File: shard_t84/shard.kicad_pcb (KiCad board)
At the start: 2 copper layers, 35 x 25 mm, 8 parts, among them J0 Shard, J1 ISP, U1 ATtiny84-20PU

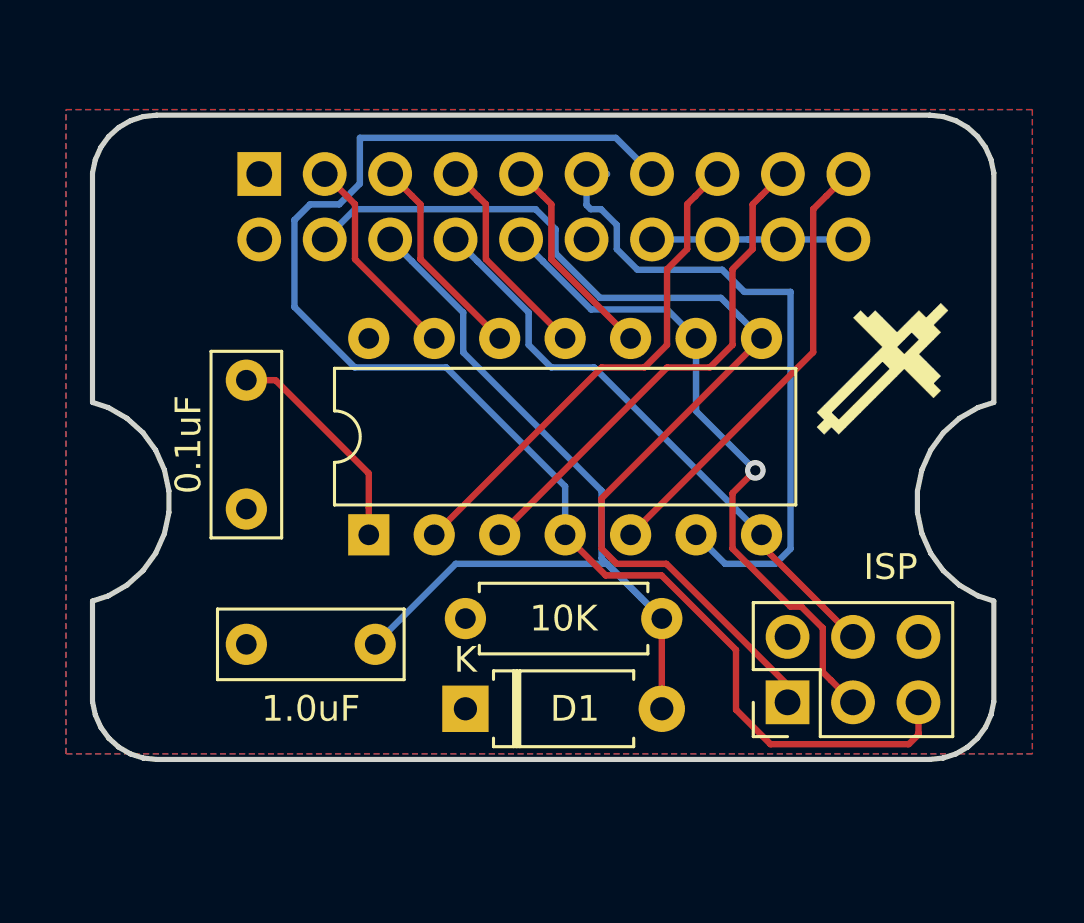
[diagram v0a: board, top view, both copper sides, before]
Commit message: reworked board for correct connector orientation
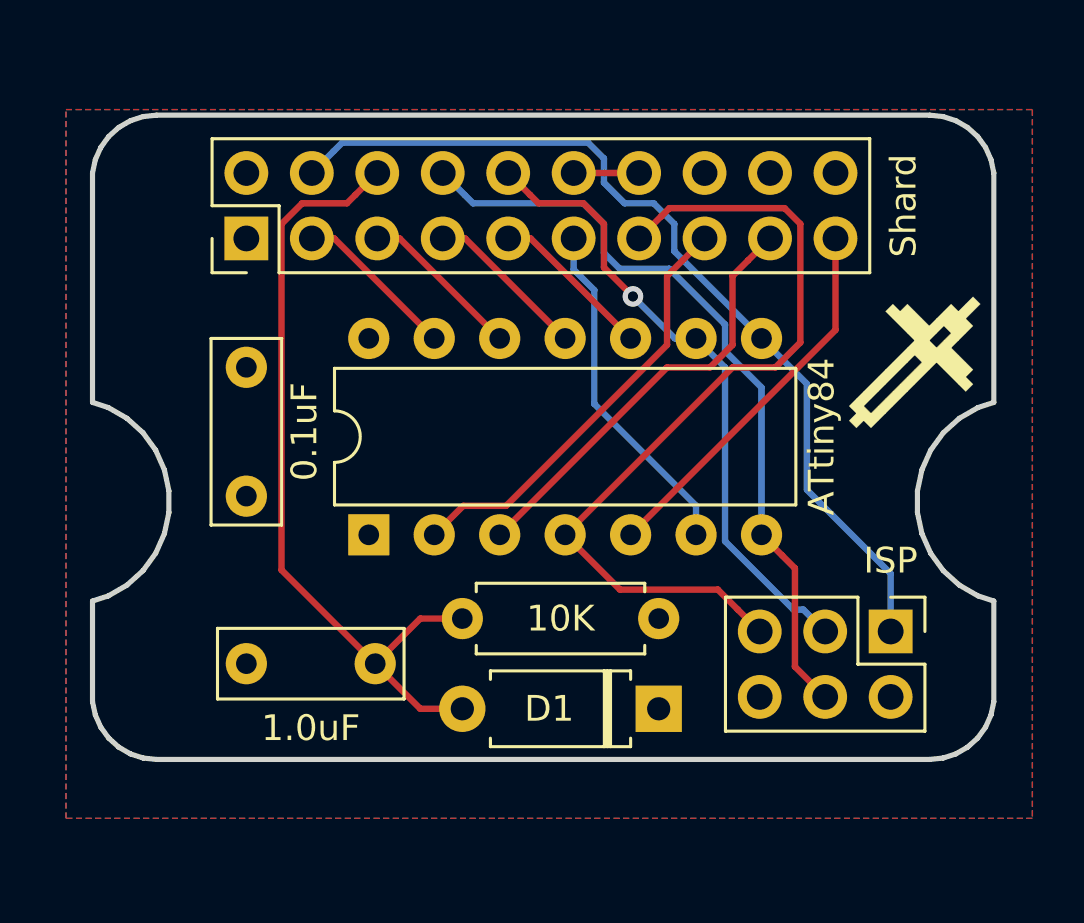
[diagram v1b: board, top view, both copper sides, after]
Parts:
- J0: moved to F.Cu
- U1: value ATtiny84-20PU -> ATtiny84
- moved D1 7.50 mm to (140.5, 75.8), turned to 180 degrees
- moved R1 7.50 mm to (140.5, 72.2), turned to 180 degrees
- moved J1 4.85 mm to (149.5, 72.8), turned to 270 degrees
- moved C0 4.50 mm to (124.5, 67.5), turned to 90 degrees
- moved J0 2.55 mm to (124.5, 57.5), turned to 90 degrees
- moved SPIKE 1.27 mm to (151.0, 57.5)
- moved C1 0.75 mm to (124.5, 74.0)
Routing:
- net RESET: track 55.3 -> 32.9 mm
- net SND: track 26.2 -> 13.5 mm
- net +3V3: track 8.63 -> 0.00 mm
- net D_MOSI: track 22.8 -> 30.1 mm
- net D_DC: track 40.9 -> 35.7 mm
- net GND: track 7.62 -> 2.54 mm
- net D_RST: track 35.9 -> 31.3 mm
- net BTN_A: track 17.5 -> 14.8 mm
- net BTN_B: track 19.5 -> 16.8 mm
- net BTN_C: track 19.5 -> 16.8 mm
- net DOWN: track 8.14 -> 6.36 mm
- net UP: track 8.14 -> 6.36 mm
- net RIGHT: track 8.14 -> 6.36 mm
- net LEFT: track 8.14 -> 6.36 mm
- net D_SCK: track 26.0 -> 24.6 mm
- added copper zone on F.Cu, net +3V3
- added copper zone on B.Cu, net GND
- removed copper zone on B.Cu, net +3V3
- removed copper zone on F.Cu, net GND

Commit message: t84 shard updated for new layout
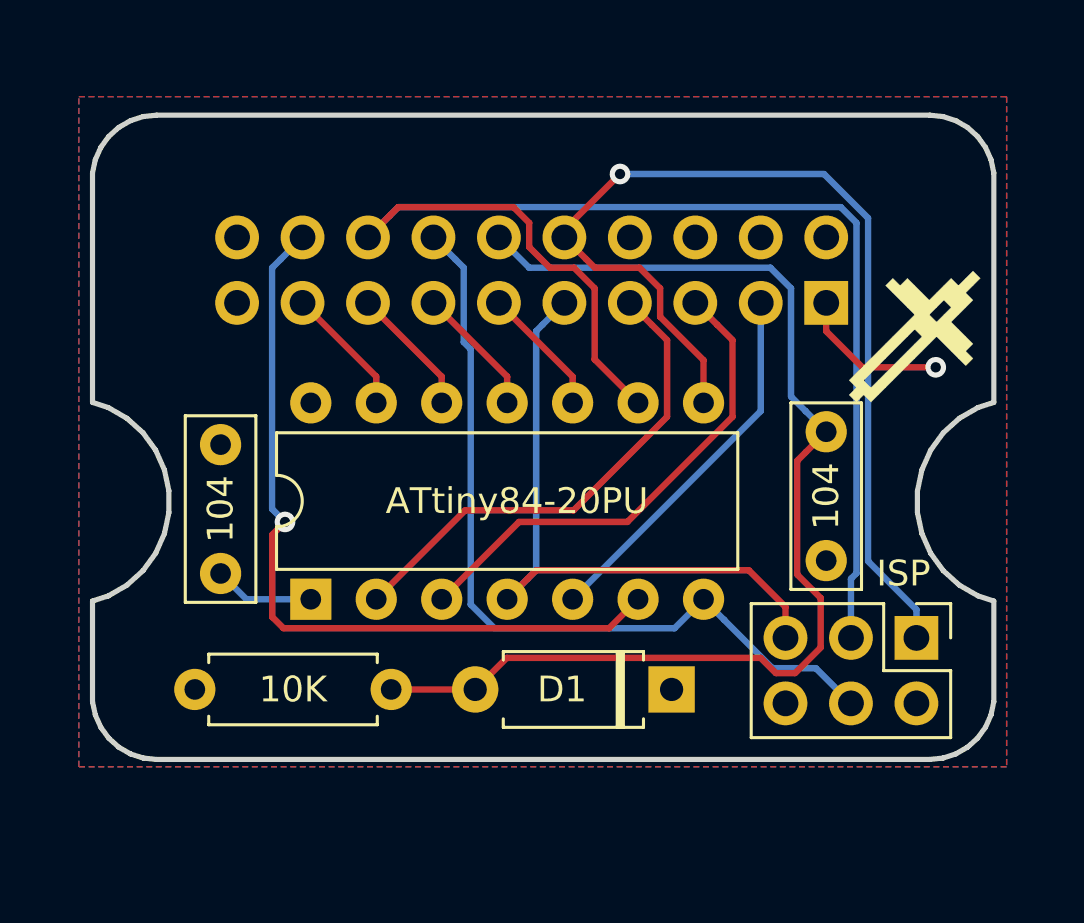
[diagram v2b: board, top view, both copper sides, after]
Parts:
- C0: value 0.1uF -> 104
- C1: value 1.0uF -> 104
- J0: moved to B.Cu
- U1: value ATtiny84 -> ATtiny84-20PU
- moved C1 22.9 mm to (147.0, 70.0), turned to 90 degrees
- moved J0 22.6 mm to (147.0, 60.0)
- moved R1 18.2 mm to (122.5, 75.0), turned to 0 degrees
- moved U1 3.36 mm to (127.0, 71.5)
- moved C0 3.16 mm to (123.5, 70.5)
- moved J1 1.03 mm to (150.5, 73.0)
- moved SPIKE 1.00 mm to (151.0, 56.5)
- moved D1 0.90 mm to (141.0, 75.0)
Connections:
- J0 pad 10: D_SCK -> D_DC
- J0 pad 11: SND -> UP
- J0 pad 12: GND -> D_RST
- J0 pad 13: RESET -> RIGHT
- J0 pad 14: GND -> D_MOSI
- J0 pad 15: BTN_C -> LEFT
- J0 pad 16: GND -> D_SCK
- J0 pad 17: BTN_B -> DOWN
- J0 pad 18: GND -> SND
- J0 pad 19: BTN_A -> GND
- J0 pad 20: GND -> +3V3
- J0 pad 3: UP -> BTN_A
- J0 pad 4: D_DC -> GND
- J0 pad 5: DOWN -> BTN_B
- J0 pad 6: D_RST -> GND
- J0 pad 7: LEFT -> BTN_C
- J0 pad 8: D_MOSI -> GND
- J0 pad 9: RIGHT -> RESET
- U1 pad 10: RIGHT -> UP
- U1 pad 11: LEFT -> RIGHT
- U1 pad 12: DOWN -> LEFT
- U1 pad 13: UP -> DOWN
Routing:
- net D_SCK: track 24.6 -> 52.2 mm, vias 1 -> 0
- net SND: track 13.5 -> 30.5 mm, vias 0 -> 1
- net D_RST: track 31.3 -> 45.3 mm
- net +3V3: track 0.00 -> 9.84 mm, vias 0 -> 1
- net RESET: track 32.9 -> 25.5 mm
- net D_DC: track 35.7 -> 40.4 mm, vias 0 -> 1
- net GND: track 2.54 -> 0.00 mm
- net BTN_B: track 16.8 -> 19.2 mm
- net BTN_C: track 16.8 -> 19.2 mm
- net D_MOSI: track 30.1 -> 32.1 mm
- net DOWN: track 6.36 -> 5.06 mm
- net UP: track 6.36 -> 5.06 mm
- net RIGHT: track 6.36 -> 5.06 mm
- net LEFT: track 6.36 -> 5.06 mm
- added copper zone on B.Cu, net +3V3
- added copper zone on F.Cu, net GND
- removed copper zone on F.Cu, net +3V3
- removed copper zone on B.Cu, net GND

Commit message: updated for edge connector
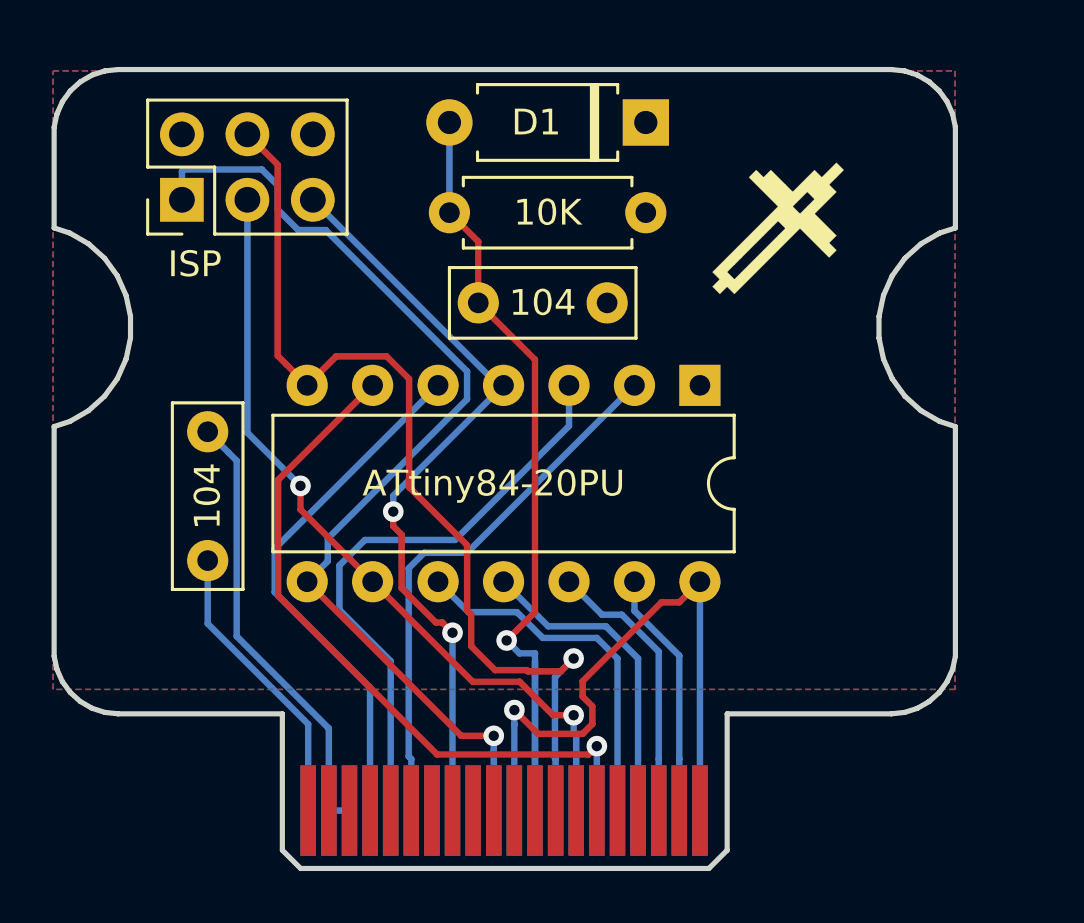
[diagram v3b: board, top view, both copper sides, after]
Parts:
- J0: footprint Connector_PinHeader_2.54mm:PinHeader_2x10_P2.54mm_Vertical -> Custom Footprints:Samtec_MEC8-120-02-L-D-RA1_Edge; moved to F.Cu
- moved J1 33.2 mm to (122.0, 56.0), turned to 90 degrees
- moved J0 29.3 mm to (126.9, 81.3), turned to 0 degrees
- moved R1 25.5 mm to (140.0, 56.5), turned to 180 degrees
- moved D1 22.0 mm to (140.0, 53.0)
- moved U1 17.2 mm to (142.1, 63.2), turned to 270 degrees
- moved C1 13.1 mm to (138.5, 60.0), turned to 180 degrees
- moved SPIKE 6.76 mm to (145.7, 52.3)
- moved C0 0.71 mm to (123.0, 70.0)
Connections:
- J0 pad 1: +3V3 -> Net-(J0-Pad1)
- J0 pad 10: D_DC -> BTN_B
- J0 pad 11: UP -> Net-(J0-Pad11)
- J0 pad 12: D_RST -> BTN_C
- J0 pad 13: RIGHT -> Net-(J0-Pad13)
- J0 pad 14: D_MOSI -> Net-(J0-Pad14)
- J0 pad 15: LEFT -> Net-(J0-Pad15)
- J0 pad 16: D_SCK -> RESET
- J0 pad 17: DOWN -> Net-(J0-Pad17)
- J0 pad 18: SND -> Net-(J0-Pad18)
- J0 pad 19: GND -> Net-(J0-Pad19)
- J0 pad 2: GND -> +3V3
- J0 pad 20: +3V3 -> D_DC
- J0 pad 3: BTN_A -> Net-(J0-Pad3)
- J0 pad 5: BTN_B -> Net-(J0-Pad5)
- J0 pad 7: BTN_C -> Net-(J0-Pad7)
- J0 pad 8: GND -> BTN_A
- J0 pad 9: RESET -> Net-(J0-Pad9)
- U1 pad 11: RIGHT -> DOWN
- U1 pad 13: DOWN -> RIGHT
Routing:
- net GND: track 0.00 -> 41.8 mm, vias 0 -> 1
- net D_SCK: track 52.2 -> 30.5 mm, vias 0 -> 2
- net D_RST: track 45.3 -> 35.1 mm, vias 0 -> 1
- net UP: track 5.06 -> 14.1 mm
- net DOWN: track 5.06 -> 12.4 mm
- net BTN_A: track 14.5 -> 20.7 mm
- net LEFT: track 5.06 -> 10.8 mm
- net D_MOSI: track 32.1 -> 37.7 mm, vias 0 -> 1
- net RIGHT: track 5.06 -> 9.60 mm
- net RESET: track 25.5 -> 29.8 mm, vias 0 -> 2
- net BTN_B: track 19.2 -> 23.1 mm
- net SND: track 30.5 -> 27.4 mm
- net BTN_C: track 19.2 -> 21.1 mm
- net +3V3: track 9.84 -> 11.3 mm, vias 1 -> 0
- net D_DC: track 40.4 -> 39.3 mm
- added copper zone on F.Cu, net +3V3
- added copper zone on B.Cu, net GND
- removed copper zone on B.Cu, net +3V3
- removed copper zone on F.Cu, net GND
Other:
- board size 35 x 25 mm -> 35 x 31 mm

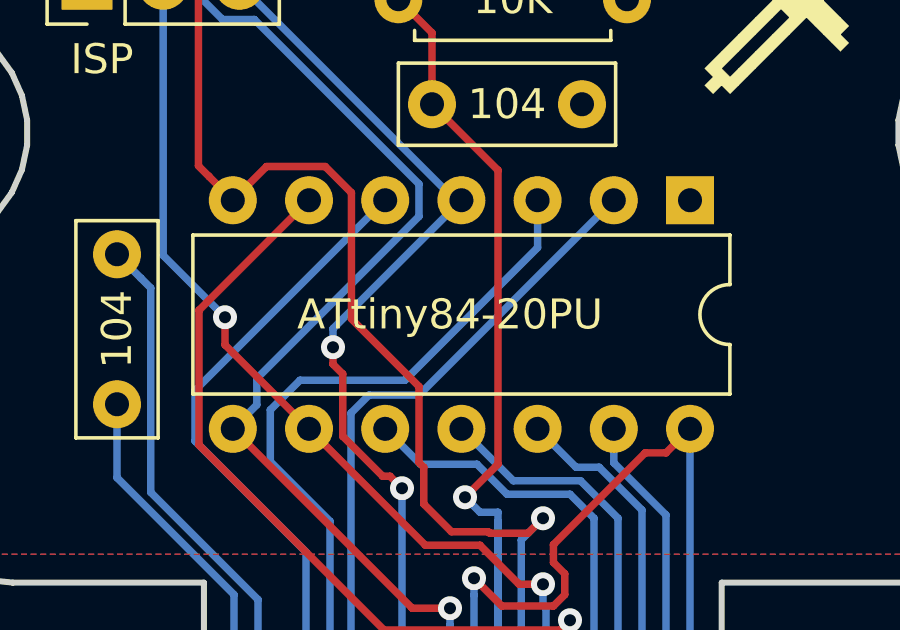
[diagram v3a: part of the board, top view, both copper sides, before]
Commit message: tweaked labels
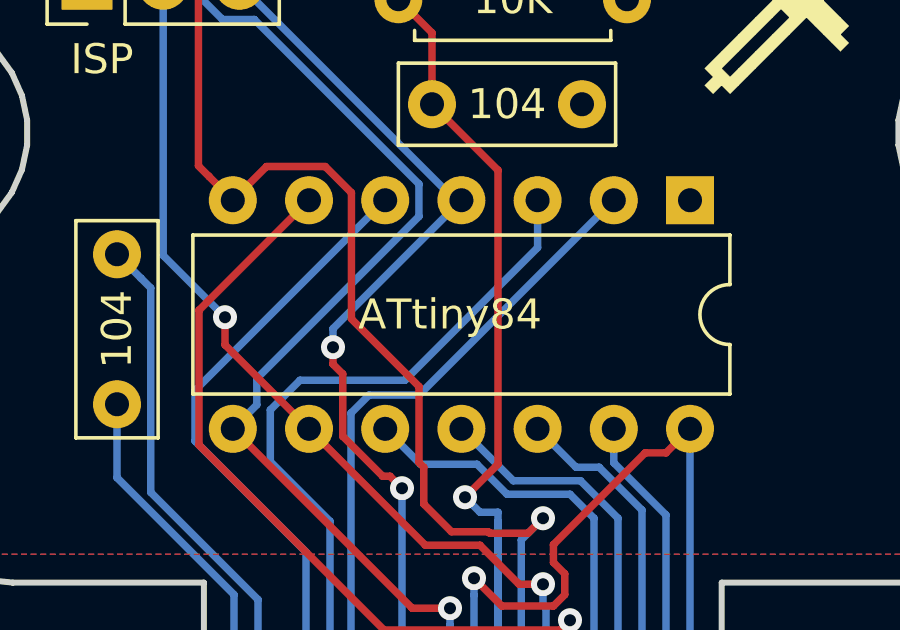
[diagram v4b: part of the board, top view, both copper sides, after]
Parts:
- U1: value ATtiny84-20PU -> ATtiny84
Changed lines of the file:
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@@
-(kicad_pcb (version 20171130) (host pcbnew "(5.0.1-3-g963ef8bb5)")
+(kicad_pcb (version 20171130) (host pcbnew "(5.0.0)")
   (general
     (thickness 1.6)
@@
     (solder_mask_min_width 0.25)
     (aux_axis_origin 0 0)
-    (visible_elements FFFFFF7F)
+    (visible_elements 7FFFFFFF)
     (pcbplotparams
       (layerselection 0x010fc_ffffffff)
@@
       (outputformat 1)
       (mirror false)
-      (drillshape 1)
+      (drillshape 0)
       (scaleselection 1)
-      (outputdirectory ""))
+      (outputdirectory "../../../Scratch/Spike_Gerbers/Shard_t84/"))
   )
   (net 0 "")
@@
       (effects (font (size 1 1) (thickness 0.15)))
     )
-    (fp_text value ATtiny84-20PU (at 3.81 8) (layer F.SilkS)
+    (fp_text value ATtiny84 (at 3.81 8) (layer F.SilkS)
       (effects (font (size 1 1) (thickness 0.15)))
     )
@@
   (gr_line (start 151.4 64.6) (end 150.6758 64.18188) (layer Edge.Cuts) (width 0.2))
   (gr_line (start 145.2 57.1) (end 143.45 58.85) (layer F.Mask) (width 0.5))
-  (via (at 134.9 75.8) (size 0.8) (drill 0.4) (layers F.Cu B.Cu) (net 15))
   (segment (start 123 71.13137) (end 123 70) (width 0.25) (layer B.Cu) (net 1))
   (segment (start 123 72.447806) (end 123 71.13137) (width 0.25) (layer B.Cu) (net 1))
   (segment (start 126.9 76.347806) (end 123 72.447806) (width 0.25) (layer B.Cu) (net 1))
   (segment (start 126.9 79.7) (end 126.9 76.347806) (width 0.25) (layer B.Cu) (net 1))
-  (via (at 132.5 72.8) (size 0.8) (drill 0.4) (layers F.Cu B.Cu) (net 11))
-  (via (at 126.6 67.1) (size 0.8) (drill 0.4) (layers F.Cu B.Cu) (net 9))
-  (via (at 138.1 77.2) (size 0.8) (drill 0.4) (layers F.Cu B.Cu) (net 10))
   (segment (start 138.10002 73.00002) (end 138.9 73.8) (width 0.25) (layer B.Cu) (net 2))
   (segment (start 138.9 73.8) (end 138.9 79.7) (width 0.25) (layer B.Cu) (net 2))
@@
   (segment (start 139.56 71.95137) (end 141.3 73.69137) (width 0.25) (layer B.Cu) (net 8))
   (segment (start 139.56 70.82) (end 139.56 71.95137) (width 0.25) (layer B.Cu) (net 8))
+  (via (at 126.6 67.1) (size 0.8) (drill 0.4) (layers F.Cu B.Cu) (net 9))
   (via (at 137.2 76) (size 0.8) (drill 0.4) (layers F.Cu B.Cu) (net 9))
   (segment (start 137.3 76.8) (end 137.3 79.7) (width 0.25) (layer B.Cu) (net 9))
@@
   (segment (start 136.4 76) (end 137.2 76) (width 0.25) (layer F.Cu) (net 9))
   (segment (start 135.1 74.7) (end 136.4 76) (width 0.25) (layer F.Cu) (net 9))
+  (via (at 138.1 77.2) (size 0.8) (drill 0.4) (layers F.Cu B.Cu) (net 10))
   (segment (start 125.734999 71.360001) (end 131.899999 77.525001) (width 0.25) (layer F.Cu) (net 10))
   (segment (start 125.734999 66.865001) (end 125.734999 71.360001) (width 0.25) (layer F.Cu) (net 10))
@@
   (segment (start 137.774999 77.525001) (end 138.1 77.2) (width 0.25) (layer F.Cu) (net 10))
   (segment (start 138.1 79.7) (end 138.1 77.2) (width 0.25) (layer B.Cu) (net 10))
+  (via (at 132.5 72.8) (size 0.8) (drill 0.4) (layers F.Cu B.Cu) (net 11))
   (segment (start 134.28 63.2) (end 134.48 63.2) (width 0.25) (layer B.Cu) (net 11))
   (segment (start 127.08 56) (end 134.28 63.2) (width 0.25) (layer B.Cu) (net 11))
@@
   (segment (start 125.6 71.225002) (end 125.6 69.54) (width 0.25) (layer B.Cu) (net 14))
   (segment (start 129.3 79.7) (end 129.3 74.925002) (width 0.25) (layer B.Cu) (net 14))
+  (via (at 134.9 75.8) (size 0.8) (drill 0.4) (layers F.Cu B.Cu) (net 15))
   (segment (start 142.1 79.7) (end 142.1 70.82) (width 0.25) (layer B.Cu) (net 15))
   (segment (start 123.799999 65.799999) (end 123 65) (width 0.25) (layer B.Cu) (net 15))
